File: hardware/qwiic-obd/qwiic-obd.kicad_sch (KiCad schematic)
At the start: 8 parts, among them J101 I2C_STANDARD, J102 DB15_Female_HighDensity, J103 I2C_STANDARD

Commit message: OK, layout v1 complete
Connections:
- net HS_CAN_HIGH is gone; now on net HS_CAN_HI: J102.6
- net MS_CAN_HIGH is gone; now on net MS_CAN_HI: J102.3

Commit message: Fix title block
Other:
- title: (none) -> QWIIC OBDII Interface
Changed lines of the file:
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@@
 (kicad_sch (version 20211123) (generator eeschema)
   (paper "A4")
+  (title_block
+    (title "QWIIC OBDII Interface")
+    (date "2023-01-03")
+  )
   (junction (at 77.47 125.73) (diameter 0) (color 0 0 0 0)
   )

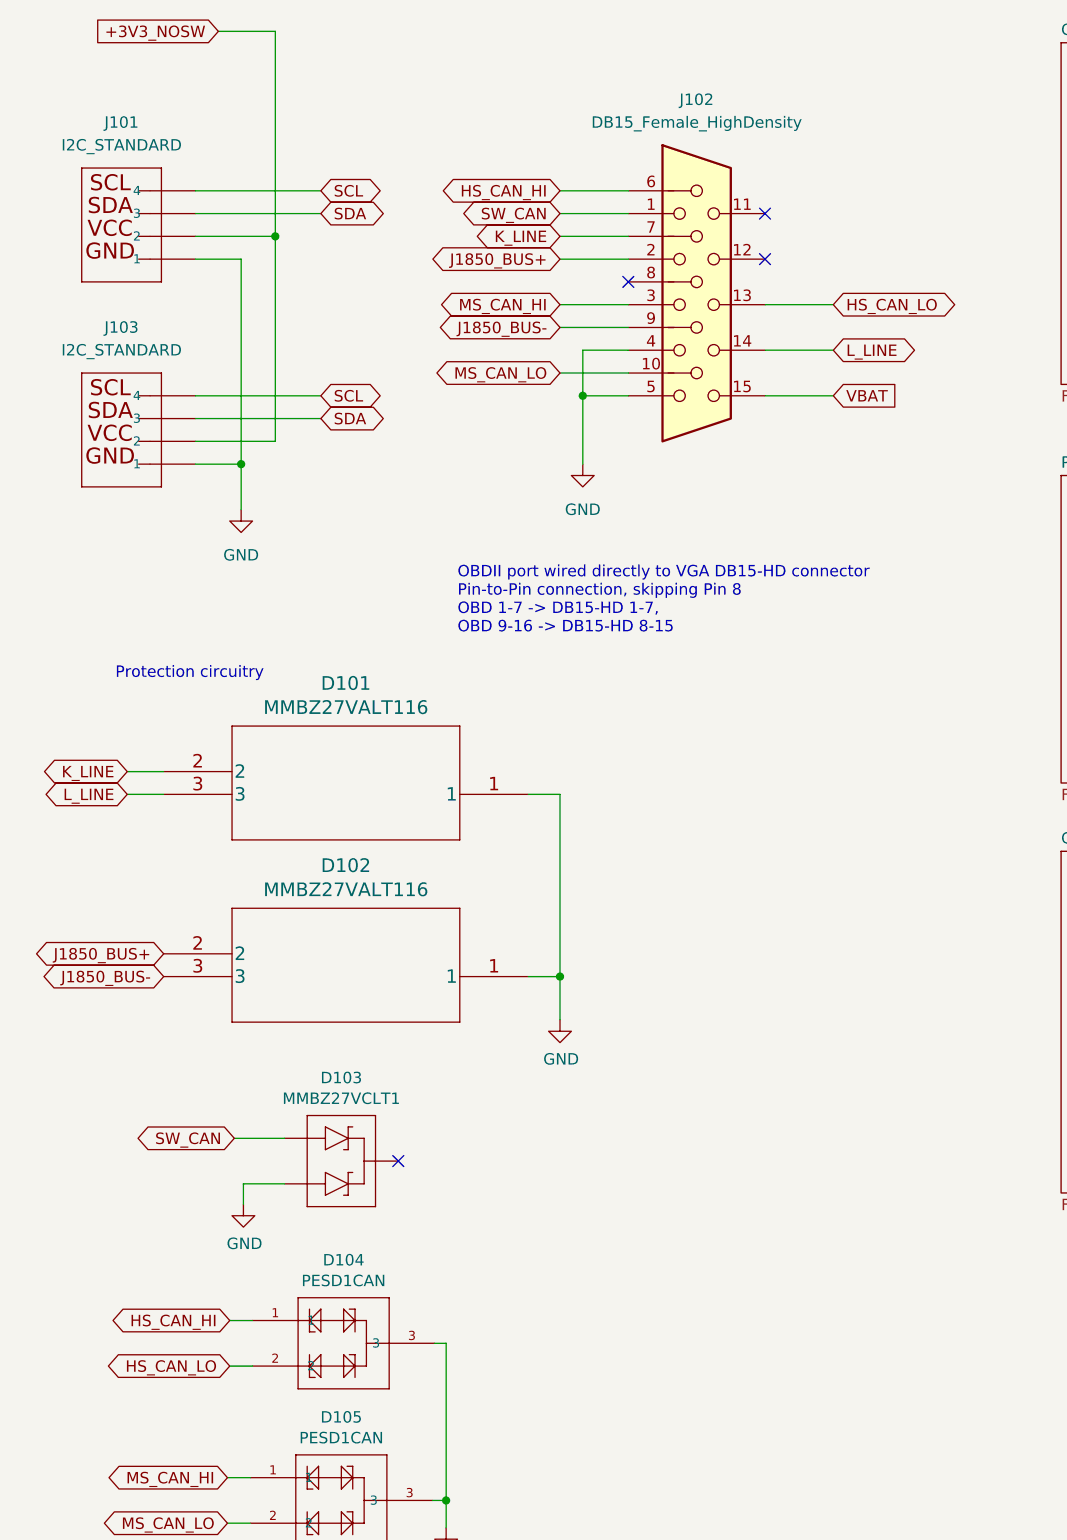
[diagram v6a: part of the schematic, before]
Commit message: Changed DB15HD connector, fixed layout
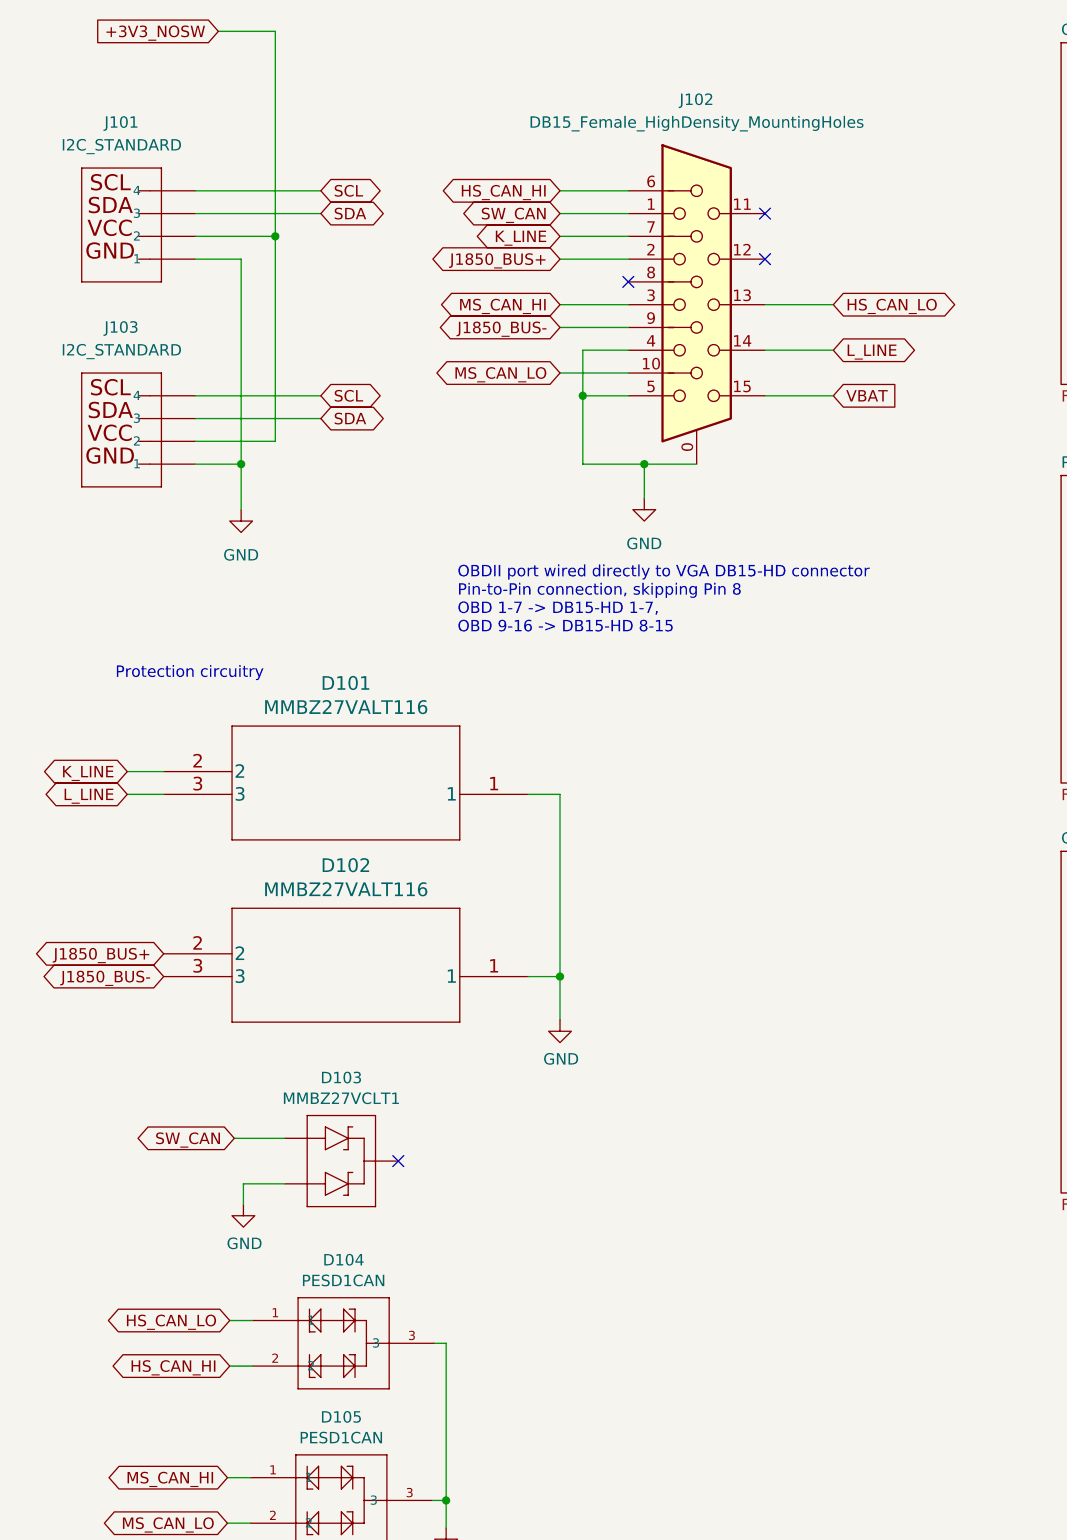
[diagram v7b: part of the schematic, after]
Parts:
- removed J102: DB15_Female_HighDensity, Connector_Dsub:DSUB-15-HD_Female_Horizontal_P2.29x2.54mm_EdgePinOffset9.40mm, symbol Connector:DB15_Female_HighDensity
- added J102: DB15_Female_HighDensity_MountingHoles, Connector_Dsub:DSUB-15-HD_Female_Horizontal_P2.29x1.98mm_EdgePinOffset8.35mm_Housed_MountingHolesOffset10.89mm, symbol Connector:DB15_Female_HighDensity_MountingHoles
- D101, D102: footprint UltraLibrarian:MMBZ27VALT116 -> SparkFun-DiscreteSemi:SOT23-3
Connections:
- net GND: now also J102.0, J102.4, J102.5
- net HS_CAN_HI: now also D104.2, J102.6; no longer D104.1
- net HS_CAN_LO: now also D104.1, J102.13; no longer D104.2
- net J1850_BUS+: now also J102.2
- net J1850_BUS-: now also J102.9
- net K_LINE: now also J102.7
- net L_LINE: now also J102.14
- net MS_CAN_HI: now also J102.3
- net MS_CAN_LO: now also J102.10
- net SW_CAN: now also J102.1
- net VBAT: now also J102.15

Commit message: Shrunk layout a bit
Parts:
- D101, D102: Digikey (none) -> MMBZ27VALT116CT-ND
- D103: Digikey (none) -> MMBZ27VCL-FDICT-ND
- D104, D105: Digikey (none) -> 1727-3817-1-ND
- J101, J103: SparkFun (none) -> PRT-16766
- J102: Digikey (none) -> L77HDE15SD1CH4FVGA-ND
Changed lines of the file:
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@@
       (effects (font (size 1.524 1.524)))
+    )
+    (property "Digikey" "MMBZ27VALT116CT-ND" (id 4) (at 73.914 125.73 0)
+      (effects (font (size 1.27 1.27)) hide)
     )
     (pin "1")
@@
     )
     (property "Datasheet" " ~" (id 3) (at 68.58 40.64 0)
+      (effects (font (size 1.27 1.27)) hide)
+    )
+    (property "Digikey" "L77HDE15SD1CH4FVGA-ND" (id 4) (at 92.71 50.8 0)
       (effects (font (size 1.27 1.27)) hide)
     )
@@
       (effects (font (size 1.524 1.524)))
     )
+    (property "Digikey" "MMBZ27VALT116CT-ND" (id 4) (at 73.914 105.41 0)
+      (effects (font (size 1.27 1.27)) hide)
+    )
     (pin "1")
     (pin "2")
@@
       (effects (font (size 1.27 1.27)) hide)
     )
+    (property "Digikey" "1727-3817-1-ND" (id 4) (at 48.26 171.704 0)
+      (effects (font (size 1.27 1.27)) hide)
+    )
     (pin "1")
     (pin "2")
@@
       (effects (font (size 1.27 1.27)) hide)
     )
+    (property "Digikey" "MMBZ27VCL-FDICT-ND" (id 4) (at 51.816 146.304 90)
+      (effects (font (size 1.27 1.27)) hide)
+    )
     (pin "1")
     (pin "2")
@@
       (effects (font (size 1.27 1.27)) hide)
     )
+    (property "Digikey" "1727-3817-1-ND" (id 4) (at 48.006 189.23 0)
+      (effects (font (size 1.27 1.27)) hide)
+    )
     (pin "1")
     (pin "2")
@@
       (effects (font (size 1.524 1.524)))
     )
+    (property "SparkFun" "PRT-16766" (id 4) (at 26.67 71.12 0)
+      (effects (font (size 1.27 1.27)) hide)
+    )
     (pin "1")
     (pin "2")
@@
     (property "Datasheet" "" (id 3) (at 26.67 48.26 0)
       (effects (font (size 1.524 1.524)))
+    )
+    (property "SparkFun" "PRT-16766" (id 4) (at 26.67 48.26 0)
+      (effects (font (size 1.27 1.27)) hide)
     )
     (pin "1")
@@
     )
     (path "/3ceb3a02-dea1-4fb7-a142-5bd34d2ae86a/88621295-63fb-4cfe-8871-ffae2778034e"
-      (reference "D602") (unit 1) (value "BAT46W") (footprint "Diode_SMD:D_SOD-123")
+      (reference "D602") (unit 1) (value "BAT46J") (footprint "Diode_SMD:D_SOD-123")
     )
     (path "/3ceb3a02-dea1-4fb7-a142-5bd34d2ae86a/1ad0c8d1-9e39-45f5-b47b-83b0e3258fd0"
-      (reference "D603") (unit 1) (value "BAT46W") (footprint "Diode_SMD:D_SOD-123")
+      (reference "D603") (unit 1) (value "BAT46J") (footprint "Diode_SMD:D_SOD-123")
     )
     (path "/3ceb3a02-dea1-4fb7-a142-5bd34d2ae86a/2a5f5ea3-bc1c-4b58-a32f-411419ea85a4"
@@
     )
     (path "/ac2cfe8d-5f01-4945-bda9-e6c47cca6b34/d7e6f421-0f72-4e9a-818f-0744ed6e5a45"
-      (reference "D701") (unit 1) (value "BAT54W") (footprint "Diode_SMD:D_SOD-123")
+      (reference "D701") (unit 1) (value "BAT54J") (footprint "Diode_SMD:D_SOD-123")
     )
     (path "/12ed1cd2-cd48-42ad-92e9-45dc067dc7b4/c92023b2-ed05-4dfb-872b-5bfe5129f51d"
@@
     )
     (path "/3ceb3a02-dea1-4fb7-a142-5bd34d2ae86a/cff9d800-9495-47fe-bb8a-4680e8ab8d47"
-      (reference "J601") (unit 1) (value "PIC ICSP") (footprint "SparkFun-Connectors:MOLEX-1X6")
+      (reference "J601") (unit 1) (value "PIC ICSP") (footprint "Connector_PinSocket_2.54mm:PinSocket_1x06_P2.54mm_Vertical")
     )
     (path "/3ceb3a02-dea1-4fb7-a142-5bd34d2ae86a/888e3439-f6a7-4af3-927f-cb56a67f6ed3"
@@
     )
     (path "/2940c1f3-5f8f-4a77-b9a5-3db797a9d050/ecb89448-fc35-443f-b4e0-dbc03003ba59"
-      (reference "U404") (unit 1) (value "ADM6320BX33ARJZ-R7") (footprint "UltraLibrarian:ADM6320BX33ARJZ-R7")
+      (reference "U404") (unit 1) (value "APX823-31W5G-7") (footprint "UltraLibrarian:ADM6320BX33ARJZ-R7")
     )
     (path "/12ed1cd2-cd48-42ad-92e9-45dc067dc7b4/c08ccba4-54e0-4632-b0fc-87976d78a399"
